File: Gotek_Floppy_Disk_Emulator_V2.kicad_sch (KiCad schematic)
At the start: 62 parts, among them J1 Power Connector, J2 OLED Display 0.91" Module, J3 USB_A, J5 Programming Connector, J6 Floppy Data Connector, Q1 MMBT2222, Q2 BSS123, Q3 BSS123, Q4 BSS123, Q5 BSS123, Q6 BSS123, Q7 BSS123, SW1 KY040 Rotary Encoder Module, SW2 DIP Switch, U1 AMS1117-3.3, U2 STM32F105RBTx, U3 STMPS2141, U4 74HCT04, Y1 8MHz

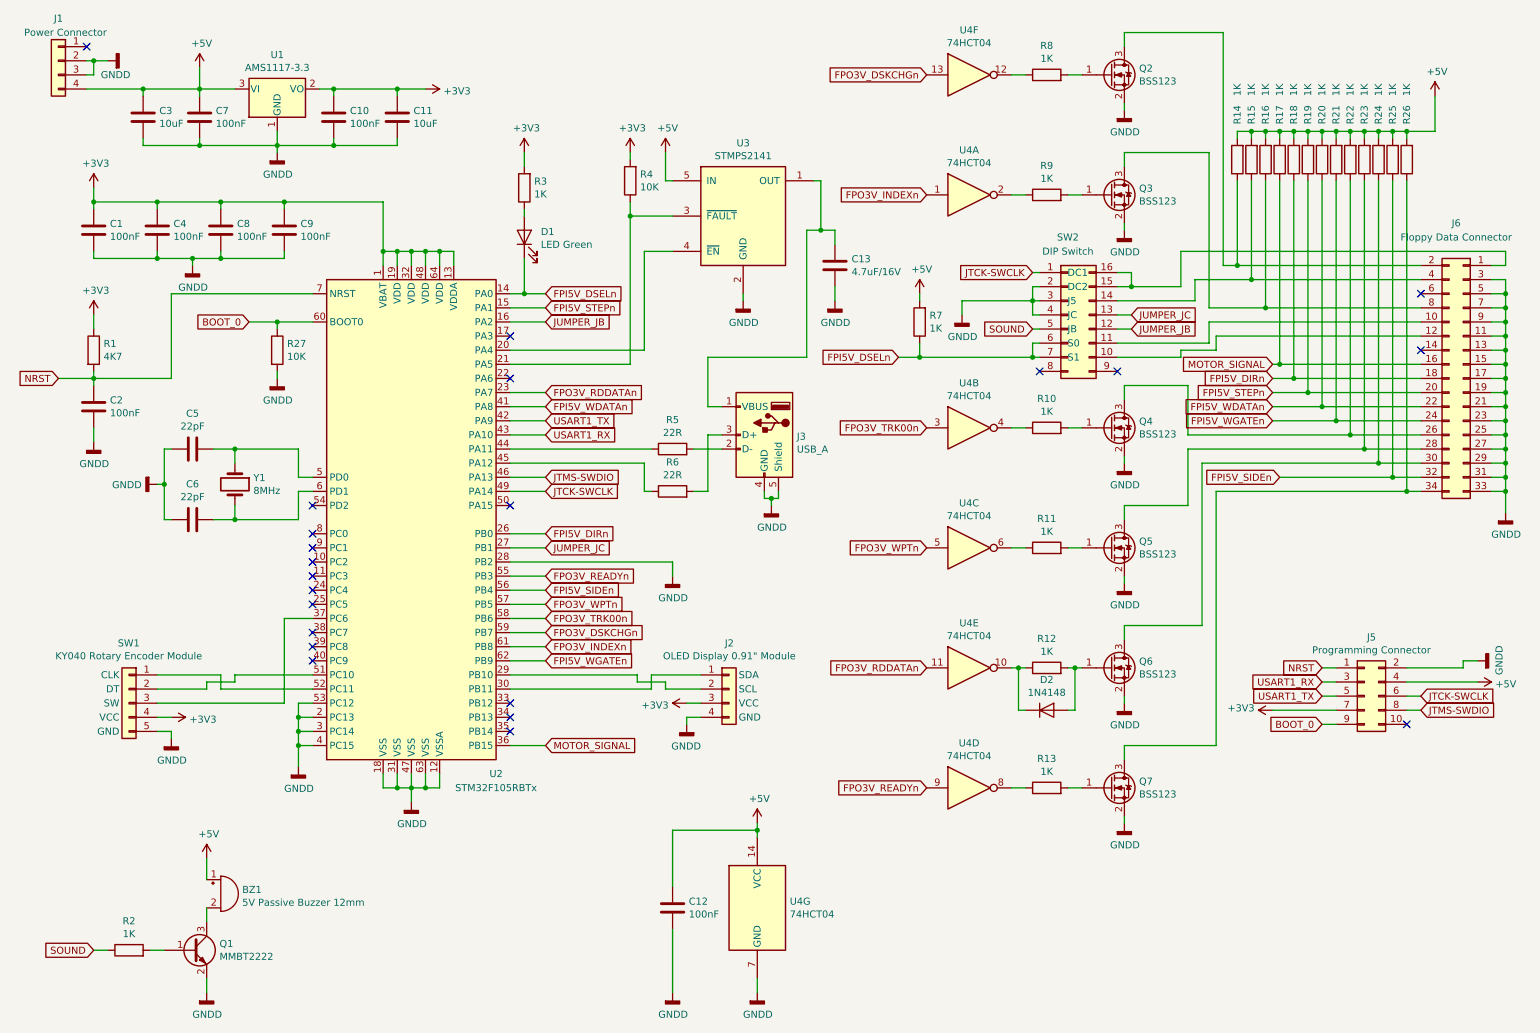
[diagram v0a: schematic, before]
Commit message: V2.1
Production files for JLCPCB excluding through hole parts and 8bit switch. Capacitors moved close to the voltage input pins of the MCU.
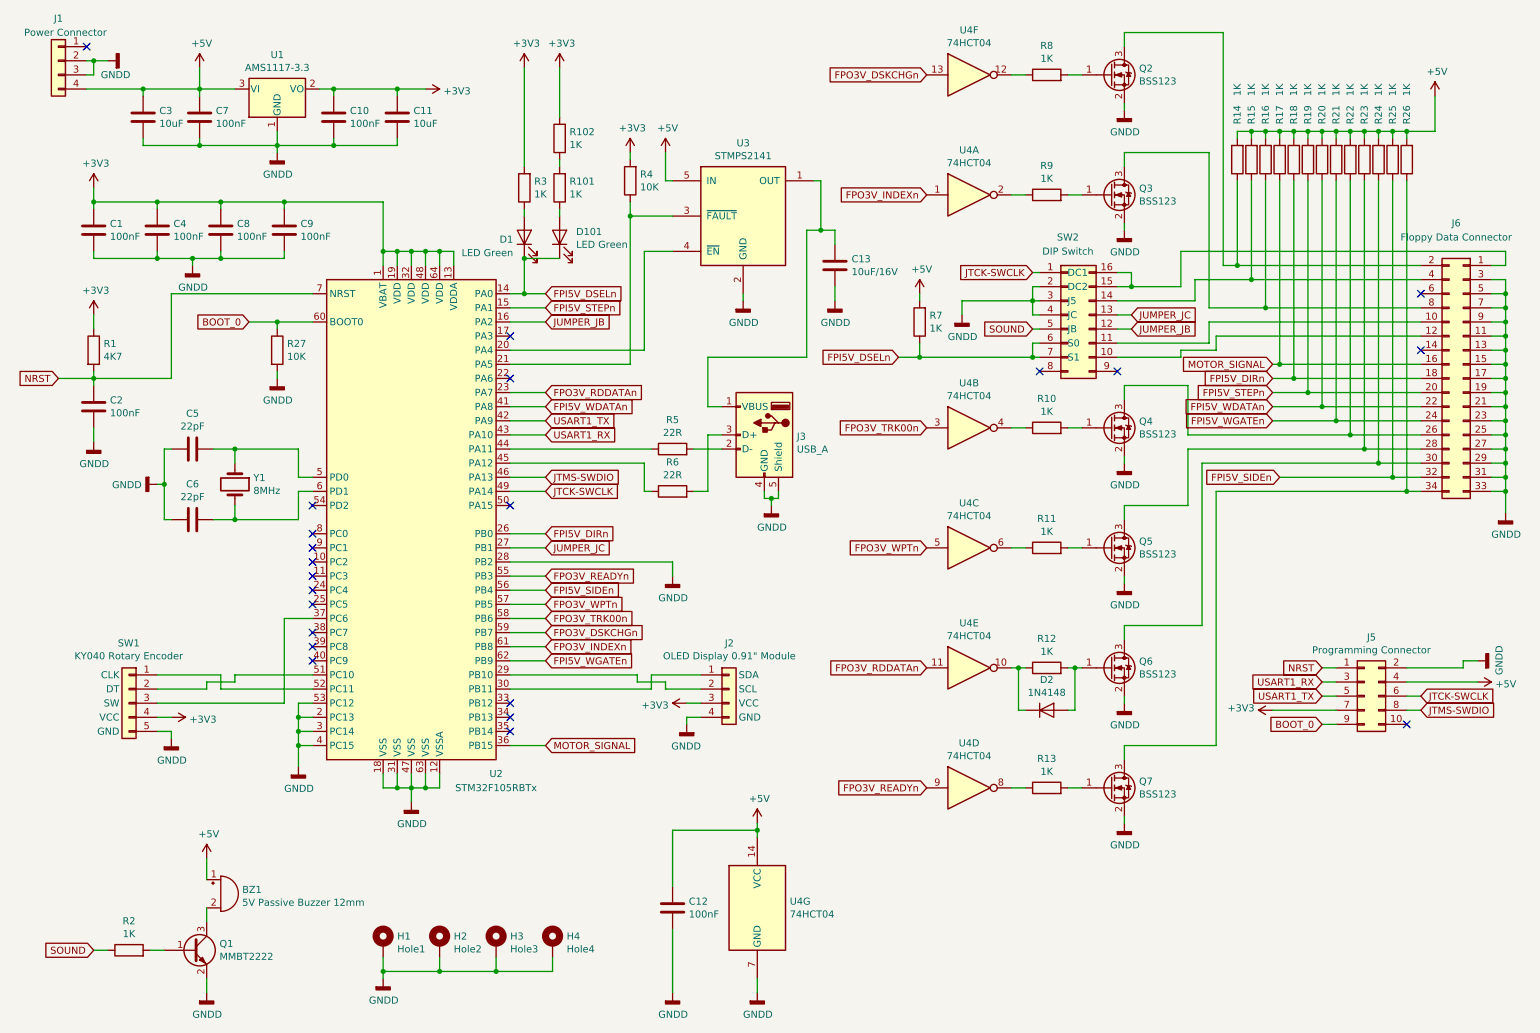
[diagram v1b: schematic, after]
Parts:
- added D101: LED Green, LED_SMD:LED_0805_2012Metric, symbol Gotek_Floppy_Disk_Emulator_V2:LED
- added H1: Hole1, MountingHole:MountingHole_3.2mm_M3_Pad_Via, symbol Mechanical:MountingHole_Pad
- added H2: Hole2, MountingHole:MountingHole_3.2mm_M3_Pad_Via, symbol Mechanical:MountingHole_Pad
- added H3: Hole3, MountingHole:MountingHole_3.2mm_M3_Pad_Via, symbol Mechanical:MountingHole_Pad
- added H4: Hole4, MountingHole:MountingHole_3.2mm_M3_Pad_Via, symbol Mechanical:MountingHole_Pad
- added R101, R102: 1K, Resistor_SMD:R_1206_3216Metric, symbol Gotek_Floppy_Disk_Emulator_V2:R
- C13: value 4.7uF/16V -> 10uF/16V
- SW1: value KY040 Rotary Encoder Module -> KY040 Rotary Encoder; footprint PinHeader_1x05_P2.54mm_Vertical -> Connector_PinHeader_2.54mm:PinHeader_1x05_P2.54mm_Vertical
- SW2: footprint SW_DIP_SPSTx08_Slide_6.7x21.88mm_W8.61mm_P2.54mm_LowProfile -> Button_Switch_SMD:SW_DIP_SPSTx08_Slide_6.7x21.88mm_W8.61mm_P2.54mm_LowProfile
- U2: footprint LQFP-64_10x10mm_P0.5mm -> Gotek_Floppy_Disk_Emulator_V2:LQFP-64_10x10mm_P0.5mm
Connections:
- net +3V3: now also R102.2
- net FPI5V_DSELn: now also D101.1 (K)
- net GNDD: now also H1.1, H2.1, H3.1, H4.1
- new net: R101.2, R102.1
- new net: D101.2 (A), R101.1
